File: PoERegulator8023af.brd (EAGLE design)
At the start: 30.5 x 33 mm, 9 parts, among them J1 SJCN

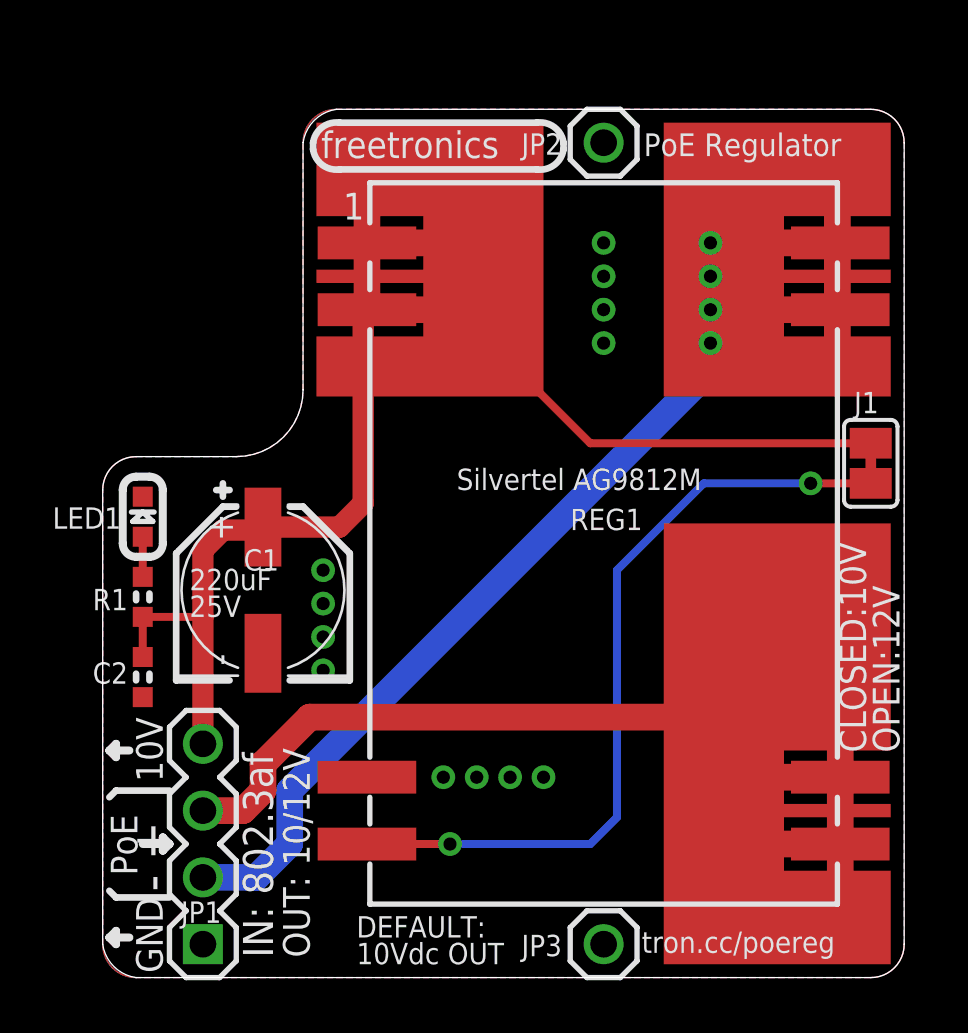
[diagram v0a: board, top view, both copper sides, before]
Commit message: Fixed fonts for silkscreen and schematic
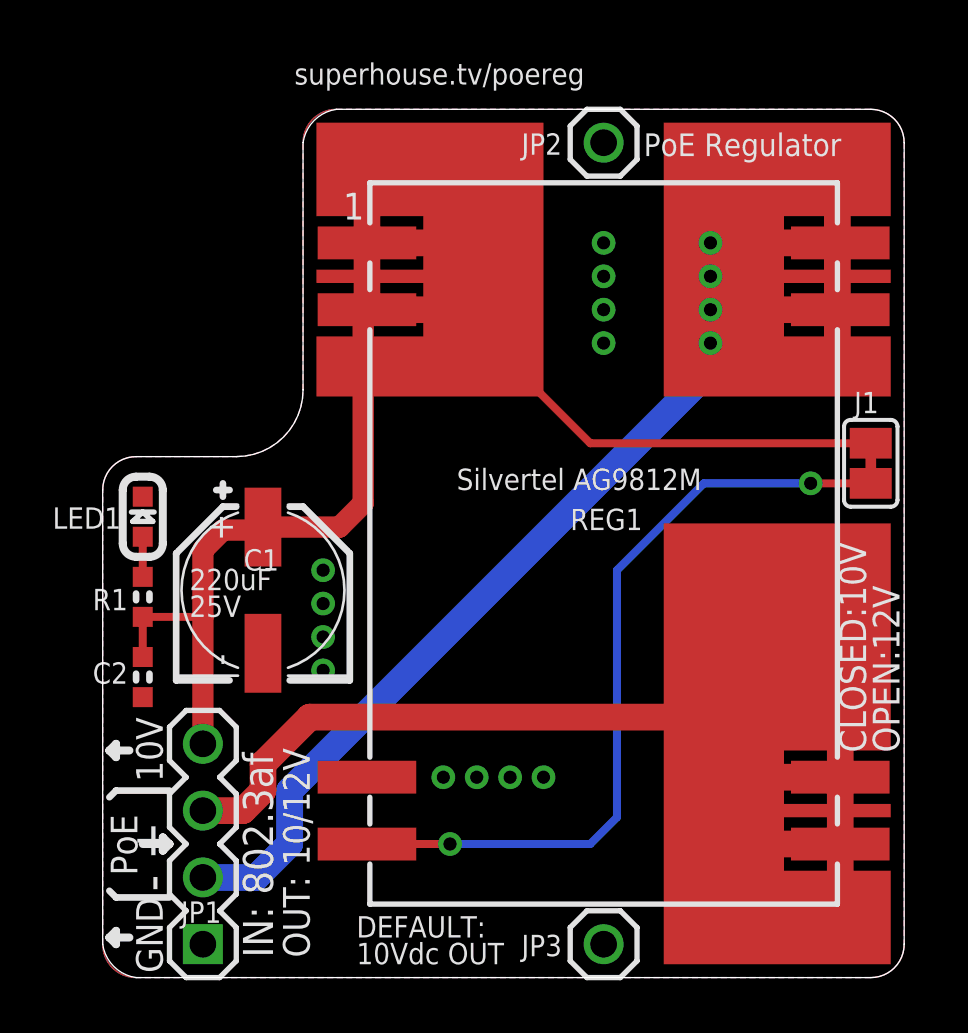
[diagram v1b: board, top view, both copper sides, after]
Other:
- board text added: "(c) 2018 SuperHouse Automation"
- board text added: "SKU: POEREG v2.1"
- board text added: "superhouse.tv/poereg"
- board text removed: "(c) 2013 Freetronics Pty Ltd"
- board text removed: "SKU: POEREG v2.0"
- board text removed: "freetronics"
- board text removed: "tron.cc/poereg"
- board text removed: "www.freetronics.com"
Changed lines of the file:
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@@
 <?xml version="1.0" encoding="utf-8"?>
 <!DOCTYPE eagle SYSTEM "eagle.dtd">
-<eagle version="6.5.0">
+<eagle version="8.5.1">
 <drawing>
 <settings>
-<setting alwaysvectorfont="yes"/>
+<setting alwaysvectorfont="no"/>
+<setting keepoldvectorfont="yes"/>
 <setting verticaltext="up"/>
 </settings>
 <grid distance="0.01" unitdist="inch" unit="inch" style="lines" multiple="1" display="no" altdistance="0.005" altunitdist="inch" altunit="inch"/>
 <layers>
-<layer number="1" name="Top" color="4" fill="1" visible="yes" active="yes"/>
+<layer number="1" name="Top" color="4" fill="1" visible="no" active="yes"/>
 <layer number="2" name="Route2" color="1" fill="3" visible="no" active="no"/>
 <layer number="3" name="Route3" color="4" fill="3" visible="no" active="no"/>
@@
 <layer number="14" name="Route14" color="1" fill="6" visible="no" active="no"/>
 <layer number="15" name="Route15" color="4" fill="6" visible="no" active="no"/>
-<layer number="16" name="Bottom" color="1" fill="1" visible="no" active="yes"/>
+<layer number="16" name="Bottom" color="1" fill="1" visible="yes" active="yes"/>
 <layer number="17" name="Pads" color="2" fill="1" visible="yes" active="yes"/>
 <layer number="18" name="Vias" color="2" fill="1" visible="yes" active="yes"/>
@@
 <layer number="20" name="Dimension" color="15" fill="1" visible="yes" active="yes"/>
 <layer number="21" name="tPlace" color="15" fill="1" visible="no" active="yes"/>
-<layer number="22" name="bPlace" color="14" fill="1" visible="no" active="yes"/>
+<layer number="22" name="bPlace" color="14" fill="1" visible="yes" active="yes"/>
 <layer number="23" name="tOrigins" color="15" fill="1" visible="no" active="yes"/>
 <layer number="24" name="bOrigins" color="15" fill="1" visible="no" active="yes"/>
@@
 <wire x1="29.21" y1="33.02" x2="8.89" y2="33.02" width="0" layer="20"/>
 <wire x1="8.89" y1="33.02" x2="7.62" y2="31.75" width="0" layer="20" curve="73.744127"/>
-<wire x1="6.985" y1="15.621" x2="6.985" y2="4.826" width="0.3048" layer="22"/>
-<wire x1="9.525" y1="4.826" x2="9.525" y2="15.621" width="0.3048" layer="22"/>
-<wire x1="9.525" y1="15.621" x2="8.509" y2="16.891" width="0.3048" layer="22" curve="89.981957"/>
-<wire x1="8.509" y1="16.891" x2="8.001" y2="16.891" width="0.3048" layer="22"/>
-<wire x1="8.001" y1="16.891" x2="6.985" y2="15.621" width="0.3048" layer="22" curve="89.981957"/>
-<wire x1="6.985" y1="4.826" x2="8.001" y2="3.556" width="0.3048" layer="22" curve="89.981957"/>
-<wire x1="8.001" y1="3.556" x2="8.509" y2="3.556" width="0.3048" layer="22"/>
-<wire x1="8.509" y1="3.556" x2="9.525" y2="4.826" width="0.3048" layer="22" curve="89.981957"/>
 <wire x1="7.62" y1="31.75" x2="7.62" y2="22.352" width="0" layer="20"/>
 <wire x1="7.62" y1="22.352" x2="5.08" y2="19.812" width="0" layer="20" curve="-90"/>
@@
 <wire x1="0.762" y1="16.51" x2="0.762" y2="18.542" width="0.3048" layer="21"/>
 <wire x1="0.762" y1="18.542" x2="1.27" y2="19.05" width="0.3048" layer="21" curve="-90"/>
-<wire x1="9.017" y1="32.512" x2="16.51" y2="32.512" width="0.254" layer="21"/>
-<wire x1="16.51" y1="30.734" x2="9.017" y2="30.734" width="0.254" layer="21"/>
-<wire x1="9.017" y1="30.734" x2="8.001" y2="31.496" width="0.254" layer="21" curve="-89.988722"/>
-<wire x1="8.001" y1="31.496" x2="8.001" y2="31.75" width="0.254" layer="21"/>
-<wire x1="8.001" y1="31.75" x2="9.017" y2="32.512" width="0.254" layer="21" curve="-89.977447"/>
-<wire x1="16.51" y1="32.512" x2="17.526" y2="31.75" width="0.254" layer="21" curve="-89.977447"/>
-<wire x1="17.526" y1="31.75" x2="17.526" y2="31.496" width="0.254" layer="21"/>
-<wire x1="17.526" y1="31.496" x2="16.51" y2="30.734" width="0.254" layer="21" curve="-89.977447"/>
 <wire x1="4.572" y1="17.907" x2="2.794" y2="16.129" width="0.254" layer="21"/>
 <wire x1="2.794" y1="16.129" x2="2.794" y2="11.303" width="0.254" layer="21"/>
@@
 <wire x1="4.318" y1="18.542" x2="4.826" y2="18.542" width="0.254" layer="21"/>
 <wire x1="4.572" y1="18.796" x2="4.572" y2="18.288" width="0.254" layer="21"/>
-<text x="11.176" y="27.432" size="1.016" layer="22" font="vector" ratio="16" rot="MR270">(c) 2013 Freetronics Pty Ltd</text>
-<text x="6.604" y="16.51" size="0.8128" layer="22" font="vector" ratio="15" rot="MR270">www.freetronics.com</text>
-<text x="8.9408" y="16.637" size="1.4224" layer="22" font="vector" ratio="17" rot="MR270">freetronics</text>
+<text x="21.59" y="30.734" size="1.1176" layer="22" font="vector" ratio="16" rot="MR270">(c) 2018 SuperHouse Automation</text>
 <text x="2.286" y="0.1778" size="1.016" layer="21" ratio="15" rot="R90">GND</text>
 <text x="2.286" y="7.4422" size="1.016" layer="21" ratio="15" rot="R90">10V</text>
@@
 <text x="1.3208" y="3.8862" size="1.016" layer="21" ratio="18" rot="R90">PoE</text>
 <text x="7.874" y="0.762" size="1.016" layer="21" ratio="18" rot="R90">OUT: 10/12V</text>
-<text x="14.605" y="18.288" size="1.27" layer="22" ratio="18" rot="MR270">tron.cc/poereg</text>
-<text x="12.7" y="21.082" size="1.016" layer="22" font="vector" ratio="16" rot="MR270">SKU: POEREG     v2.0</text>
-<text x="8.3058" y="31.1658" size="1.016" layer="21" font="vector" ratio="17">freetronics</text>
+<text x="26.035" y="22.098" size="1.524" layer="22" ratio="18" rot="MR270">superhouse.tv/poereg</text>
+<text x="23.622" y="21.082" size="1.1176" layer="22" font="vector" ratio="16" rot="MR270">SKU: POEREG     v2.1</text>
 <text x="3.937" y="17.653" size="1.016" layer="21" ratio="18" rot="R270">+</text>
 <text x="3.937" y="12.319" size="1.016" layer="21" ratio="18" rot="R270">-</text>
@@
 <rectangle x1="8.128" y1="28.956" x2="12.192" y2="32.512" layer="1"/>
 <rectangle x1="8.128" y1="26.416" x2="12.192" y2="26.924" layer="1"/>
-<text x="20.4978" y="0.9398" size="0.8128" layer="21" font="vector" ratio="17">tron.cc/poereg</text>
+<text x="7.2898" y="33.9598" size="0.8128" layer="21" font="vector" ratio="17">superhouse.tv/poereg</text>
 <text x="9.652" y="1.524" size="0.8128" layer="21" ratio="18">DEFAULT:</text>
 <text x="9.652" y="0.508" size="0.8128" layer="21" ratio="18">10Vdc OUT</text>
@@
 <param name="dpMaxLengthDifference" value="10mm"/>
 <param name="dpGapFactor" value="2.5"/>
-<param name="checkGrid" value="0"/>
 <param name="checkAngle" value="0"/>
 <param name="checkFont" value="1"/>
 <param name="checkRestrict" value="1"/>
+<param name="checkStop" value="0"/>
+<param name="checkValues" value="0"/>
 <param name="useDiameter" value="13"/>
 <param name="maxErrors" value="50"/>
@@
 <pass name="Default">
 <param name="RoutingGrid" value="50mil"/>
+<param name="AutoGrid" value="1"/>
+<param name="Efforts" value="0"/>
+<param name="TopRouterVariant" value="1"/>
 <param name="tpViaShape" value="round"/>
 <param name="PrefDir.1" value="|"/>
